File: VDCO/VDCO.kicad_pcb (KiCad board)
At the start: 2 copper layers, 37.5 x 148.9 mm, 65 parts, among them J1 Conn_02x05_Counter_Clockwise, J2 ModeCV, J3 Parameter 1 CV, J4 Parameter 2 CV, J5 Gain CV, J6 Output, J7 V/OCT, SW1 Mode Switch On-Off-On, U1 TL072

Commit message: couple changes
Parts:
- C1, C10, C11, C12, C13, C14, C15, C2, C3, C4, C5, C6, C7, C8, C9: footprint Capacitor_THT:C_Disc_D5.0mm_W2.5mm_P5.00mm -> Capacitor_SMD:C_0805_2012Metric_Pad1.18x1.45mm_HandSolder; moved to F.Cu
- D1, D10, D11, D12, D13, D3, D5, D6, D8, D9: footprint Diode_THT:D_DO-35_SOD27_P7.62mm_Horizontal -> Diode_SMD:D_0805_2012Metric_Pad1.15x1.40mm_HandSolder; moved to F.Cu
- D2, D4, D7: footprint LED_THT:LED_D5.0mm -> LED_SMD:LED_0805_2012Metric_Pad1.15x1.40mm_HandSolder
- R1, R10, R11, R12, R13, R14, R15, R16, R17, R18, R19, R2, R20, R21, R22, R23, R3, R4, R5, R6, R7, R8, R9: footprint Resistor_THT:R_Axial_DIN0207_L6.3mm_D2.5mm_P10.16mm_Horizontal -> Resistor_SMD:R_0805_2012Metric_Pad1.20x1.40mm_HandSolder; moved to F.Cu
- moved R23 57.0 mm to (21.9, 90.4)
- moved C14 35.3 mm to (36.4, 124.4), turned to 180 degrees
- moved C8 32.2 mm to (34.9, 134.7), turned to 180 degrees
- moved C15 31.8 mm to (36.4, 119.4), turned to 0 degrees
- moved D3 27.3 mm to (34.9, 132.3), turned to 180 degrees
- moved R4 26.8 mm to (34.9, 139.8)
- moved R14 25.9 mm to (39.6, 139.7)
- moved R6 25.2 mm to (35.0, 137.1)
- moved R20 24.7 mm to (36.4, 121.8), turned to 0 degrees
- moved R13 24.2 mm to (39.7, 137.2), turned to 180 degrees
- moved R18 21.4 mm to (39.8, 155.0)
- moved R5 18.9 mm to (40.2, 101.2), turned to -90 degrees
- moved R19 18.6 mm to (32.1, 121.9)
- moved R17 18.1 mm to (32.1, 119.3)
- moved D1 17.5 mm to (34.9, 130.1), turned to 0 degrees
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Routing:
- net +5V: track 158.4 -> 0.00 mm, vias 3 -> 0
- net Net-(A1-Pad26): track 146.2 -> 0.00 mm
- net Net-(A1-Pad25): track 123.2 -> 0.00 mm, vias 2 -> 0
- net Net-(A1-Pad23): track 122.2 -> 0.00 mm, vias 1 -> 0
- net Net-(A1-Pad24): track 121.8 -> 0.00 mm, vias 2 -> 0
- net Net-(A1-Pad20): track 114.9 -> 0.00 mm, vias 1 -> 0
- net +12V: track 111.4 -> 0.00 mm, vias 2 -> 0
- net Net-(A1-Pad19): track 102.4 -> 0.00 mm, vias 1 -> 0
- net Net-(A1-Pad22): track 91.7 -> 0.00 mm, vias 1 -> 0
- net Net-(R23-Pad2): track 91.0 -> 0.00 mm, vias 2 -> 0
- net Net-(C14-Pad1): track 88.0 -> 0.00 mm, vias 2 -> 0
- net -12V: track 79.2 -> 0.00 mm, vias 1 -> 0
- net Net-(A1-Pad9): track 76.6 -> 0.00 mm, vias 1 -> 0
- net Net-(R13-Pad2): track 68.8 -> 0.00 mm, vias 2 -> 0
- net Net-(A1-Pad10): track 65.1 -> 0.00 mm, vias 1 -> 0
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
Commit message: first complete routing of smd board
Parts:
- removed the D1 at (34.9, 130.1)
- removed D10, D11, D12, D13, D9: D_Schottky_Small, Diode_SMD:D_0805_2012Metric_Pad1.15x1.40mm_HandSolder
- removed the D3 at (34.9, 132.3)
- removed the D5 at (28.4, 32.6)
- added D2: D_Zener_Small, Diode_SMD:D_0805_2012Metric_Pad1.15x1.40mm_HandSolder, F.Cu at (34.2, 143.1)
- added D4: D_Zener_Small, Diode_SMD:D_0805_2012Metric_Pad1.15x1.40mm_HandSolder, F.Cu at (34.2, 136.6)
- added D7: D_Zener_Small, Diode_SMD:D_0805_2012Metric_Pad1.15x1.40mm_HandSolder, F.Cu at (34.2, 146.9)
- C13: renamed from C12; value 4.7u -> 10u
- D1: renamed from D2; footprint LED_SMD:LED_0805_2012Metric_Pad1.15x1.40mm_HandSolder -> LED_THT:LED_D5.0mm
- D3: renamed from D4; footprint LED_SMD:LED_0805_2012Metric_Pad1.15x1.40mm_HandSolder -> LED_THT:LED_D5.0mm
- D5: renamed from D7; footprint LED_SMD:LED_0805_2012Metric_Pad1.15x1.40mm_HandSolder -> LED_THT:LED_D5.0mm
- D6, D8: value D_Schottky_Small -> D_Zener_Small
- R14, R16: value 50K -> 47K
- R20: renamed from R18; value 220R -> 1K
- RV4: moved to F.Cu
- SW1: value Mode Switch On-Off-On -> SW_SPDT; footprint Button_Switch_THT:SW_CuK_JS202011CQN_DPDT_Straight -> Button_Switch_THT:SW_PUSH_6mm_H5mm
- moved R18 114.9 mm to (50.6, 145.4), turned to 180 degrees
- moved C12 111.7 mm to (25.3, 132.8), turned to 180 degrees
- moved R17 111.6 mm to (39.6, 132.3), turned to 0 degrees
- moved D6 101.2 mm to (34.1, 139.8)
- moved R8 100.4 mm to (20.6, 136.0)
- moved C10 98.2 mm to (25.3, 139.3), turned to 180 degrees
- moved R16 97.9 mm to (35.6, 157.4), turned to 180 degrees
- moved C9 97.3 mm to (25.3, 136.1), turned to 180 degrees
- moved R9 96.5 mm to (39.8, 136.5)
- moved R11 94.8 mm to (20.7, 139.3), turned to 180 degrees
- moved R12 88.0 mm to (39.8, 139.9), turned to 180 degrees
- moved R15 84.7 mm to (39.8, 146.9), turned to 180 degrees
- moved C6 83.4 mm to (25.3, 116.3)
- moved C11 82.5 mm to (25.3, 146.5), turned to 180 degrees
- moved R2 81.9 mm to (20.5, 116.4), turned to 180 degrees
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- renumbered C13 to C12, J7 to J6, J6 to J7, R21 to R17, R22 to R18, R17 to R19, R19 to R21, R20 to R22
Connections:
- A1 pad 7: Net-(A1-Pad7) -> unconnected-(A1-Pad7)
- D6 pad 1: Net-(A1-Pad23) -> Net-(A1-Pad24)
- D8 pad 1: +5V -> Net-(A1-Pad26)
- D8 pad 2: Net-(A1-Pad24) -> GND
- SW1 pad 1: Net-(A1-Pad7) -> GND
- SW1 pad 2: GND -> Net-(A1-Pad8)
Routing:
- net Net-(J6-PadT): track 0.00 -> 118.5 mm, vias 0 -> 2
- net Net-(R1-Pad2): track 0.00 -> 108.5 mm, vias 0 -> 2
- net +12V: track 0.00 -> 98.6 mm, vias 0 -> 6
- net Net-(R2-Pad2): track 0.00 -> 86.3 mm, vias 0 -> 2
- net Net-(J3-PadT): track 0.00 -> 82.4 mm, vias 0 -> 1
- net Net-(R23-Pad2): track 0.00 -> 81.3 mm, vias 0 -> 2
- net -12V: track 0.00 -> 77.7 mm, vias 0 -> 7
- net Net-(R3-Pad2): track 0.00 -> 64.9 mm, vias 0 -> 4
- net Net-(D5-Pad2): track 0.00 -> 64.4 mm, vias 0 -> 3
- net Net-(J4-PadT): track 0.00 -> 61.0 mm, vias 0 -> 2
- net Net-(D1-Pad2): track 0.00 -> 59.5 mm, vias 0 -> 3
- net Net-(RV1-Pad3): track 0.00 -> 57.2 mm
- net Net-(R20-Pad1): track 0.00 -> 55.3 mm, vias 0 -> 1
- net Net-(D3-Pad2): track 0.00 -> 46.4 mm, vias 0 -> 3
- net Net-(A1-Pad8): track 0.00 -> 46.0 mm, vias 0 -> 1
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
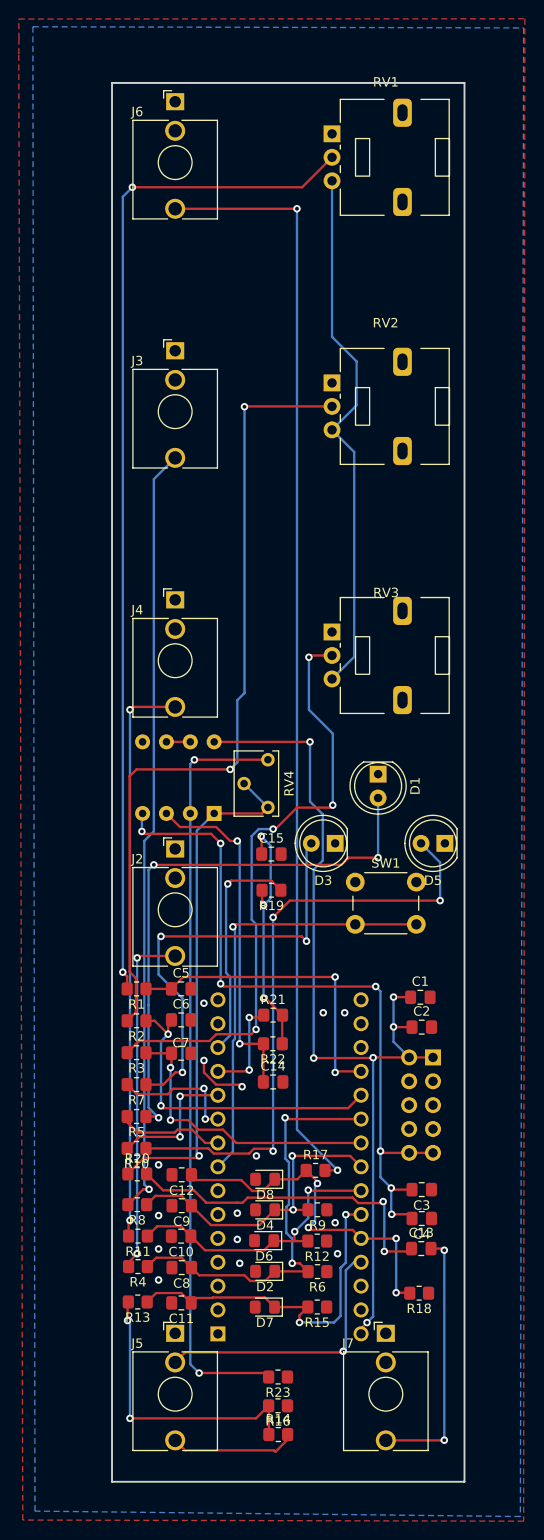
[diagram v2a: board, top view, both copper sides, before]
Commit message: remove one led, tighten up routing
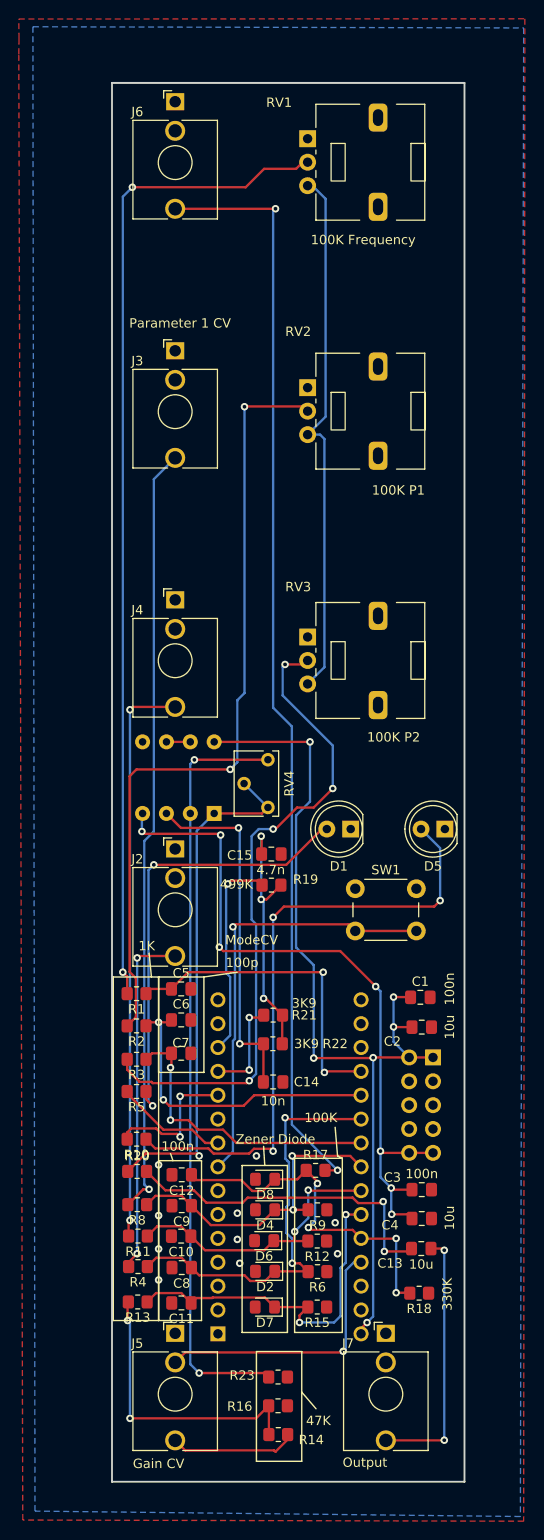
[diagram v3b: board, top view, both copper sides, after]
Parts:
- removed D3: LED, LED_THT:LED_D5.0mm
- removed R7: 1K, Resistor_SMD:R_0805_2012Metric_Pad1.20x1.40mm_HandSolder
- moved D1 6.53 mm to (43.3, 96.0), turned to 180 degrees
- moved R5 2.66 mm to (20.5, 124.0)
- moved RV3 2.65 mm to (38.7, 75.6)
- moved RV1 2.65 mm to (38.7, 22.5)
- moved RV2 2.65 mm to (38.7, 49.0)
- moved D5 1.52 mm to (53.3, 96.0)
- moved R10 0.98 mm to (20.5, 129.0)
- moved SW1 0.70 mm to (43.8, 102.4)
- moved R3 0.70 mm to (20.5, 120.5)
- moved R19 0.54 mm to (34.9, 102.0), turned to 0 degrees
- moved R2 0.54 mm to (20.5, 117.0)
- moved R1 0.51 mm to (20.5, 113.5)
- moved R20 0.26 mm to (20.6, 132.5)
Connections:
- A1 pad 10: Net-(A1-Pad10) -> unconnected-(A1-Pad10)
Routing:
- net Net-(D3-Pad2): track 46.4 -> 0.00 mm, vias 3 -> 0
- net Net-(A1-Pad10): track 13.5 -> 0.00 mm, vias 2 -> 0
- net Net-(D1-Pad2): track 59.5 -> 47.9 mm, vias 3 -> 2
- net GND: track 5.97 -> 0.00 mm, vias 15 -> 10
- net Net-(R3-Pad2): track 64.9 -> 70.2 mm
- net Net-(A1-Pad13): track 24.4 -> 22.2 mm
- net Net-(R1-Pad2): track 108.5 -> 106.4 mm
- net Net-(R2-Pad2): track 86.3 -> 84.2 mm
- net Net-(D5-Pad2): track 64.4 -> 66.4 mm
- net -12V: track 77.7 -> 76.1 mm
- net Net-(A1-Pad9): track 10.7 -> 12.1 mm
- net Net-(A1-Pad20): track 34.5 -> 33.2 mm
- net Net-(J6-PadT): track 118.5 -> 117.3 mm
- net Net-(A1-Pad19): track 33.6 -> 34.6 mm
- net Net-(C14-Pad1): track 37.1 -> 37.9 mm
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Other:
- board text added: "100K"
- board text added: "100n"
- board text added: "100p"
- board text added: "1K"
- board text added: "47K"
- board text added: "Zener Diode"
